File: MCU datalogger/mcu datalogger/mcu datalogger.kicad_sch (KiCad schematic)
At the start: 25 parts, among them U1 24LC1025, U2 DS1337S_, U3 24LC1025, U4 ATMEGA328P-AU, Y1 32.768 KHz, Y2 16MHz

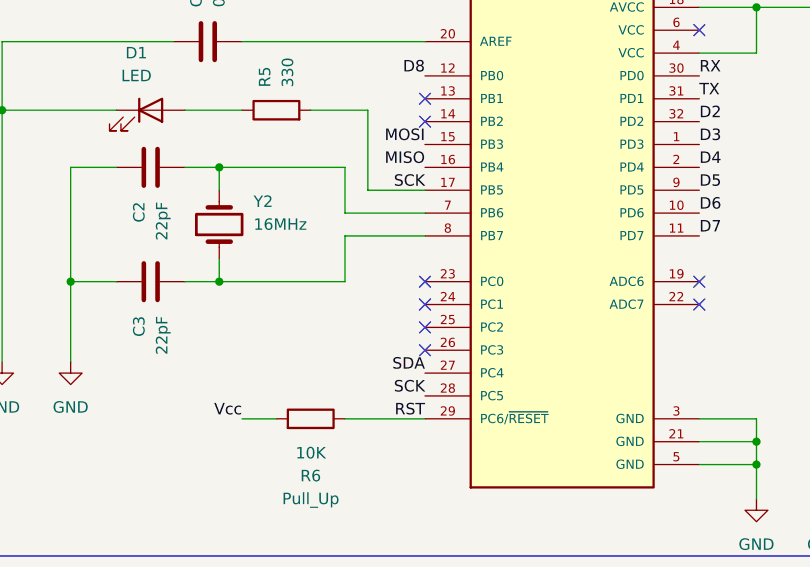
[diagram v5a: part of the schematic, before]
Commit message: Done routing the tracks.
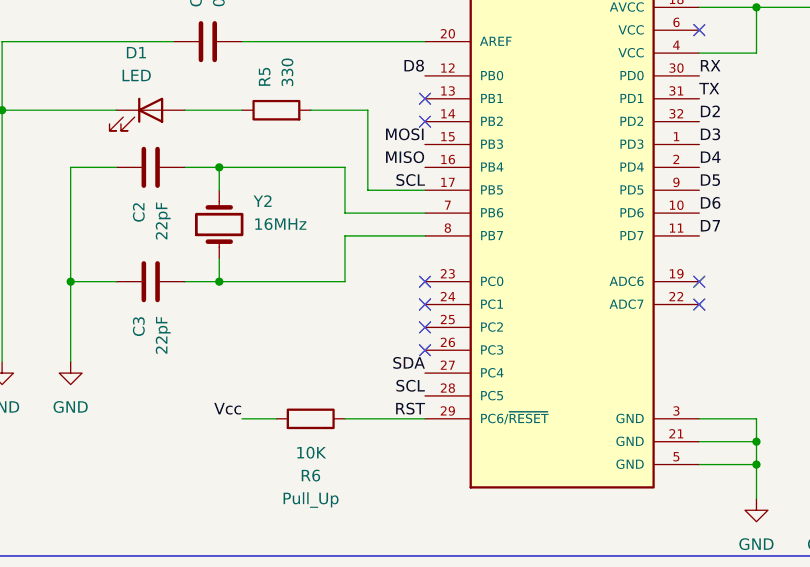
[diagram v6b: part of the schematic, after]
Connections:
- net SCK is gone; now on net SCL: R5.2, U4.17 (PB5), U4.28 (PC5)
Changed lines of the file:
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@@
     (effects (font (size 1.27 1.27)) (justify right bottom))
   )
-  (label "SCK" (at 190.5 83.82 180) (fields_autoplaced)
+  (label "SCL" (at 190.5 83.82 180) (fields_autoplaced)
     (effects (font (size 1.27 1.27)) (justify right bottom))
   )
@@
     (effects (font (size 1.27 1.27)) (justify right bottom))
   )
-  (label "SCK" (at 190.5 60.96 180) (fields_autoplaced)
+  (label "SCL" (at 190.5 60.96 180) (fields_autoplaced)
     (effects (font (size 1.27 1.27)) (justify right bottom))
   )

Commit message: Fixed outstanding issues.
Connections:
- net Vcc: now also BT1.1 (+), C5.1, D2.2 (A), U4.18 (AVCC), U4.4 (VCC)
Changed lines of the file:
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@@
     (effects (font (size 1.27 1.27)) (justify right bottom))
+  )
+  (label "Vcc" (at 248.92 40.64 0) (fields_autoplaced)
+    (effects (font (size 1.27 1.27)) (justify left bottom))
   )
   (label "TX" (at 139.7 139.7 180) (fields_autoplaced)
